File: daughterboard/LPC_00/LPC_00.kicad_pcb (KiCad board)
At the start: 4 copper layers, 67 x 50 mm, 2 parts, among them J1 m2_keyA_67pin_daughterboard

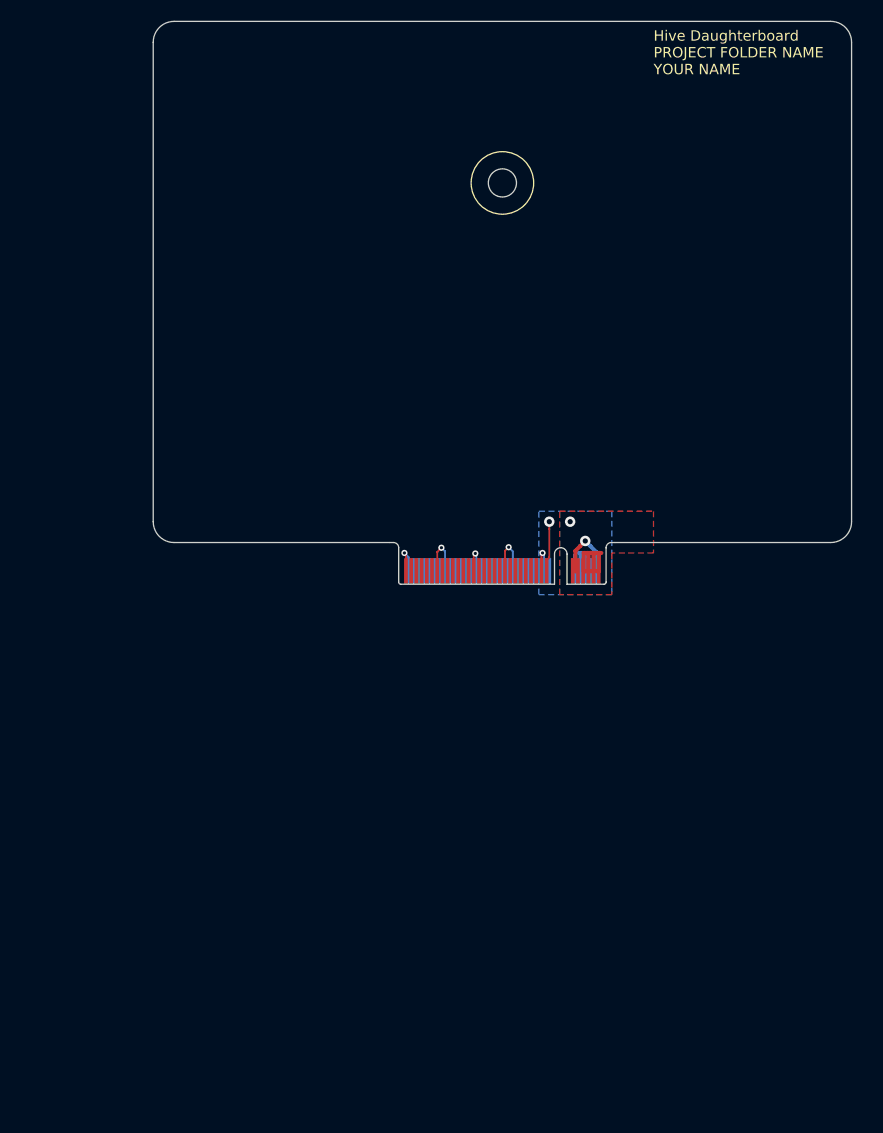
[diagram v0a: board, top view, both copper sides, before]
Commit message: sarted with LPC daughterboard layout
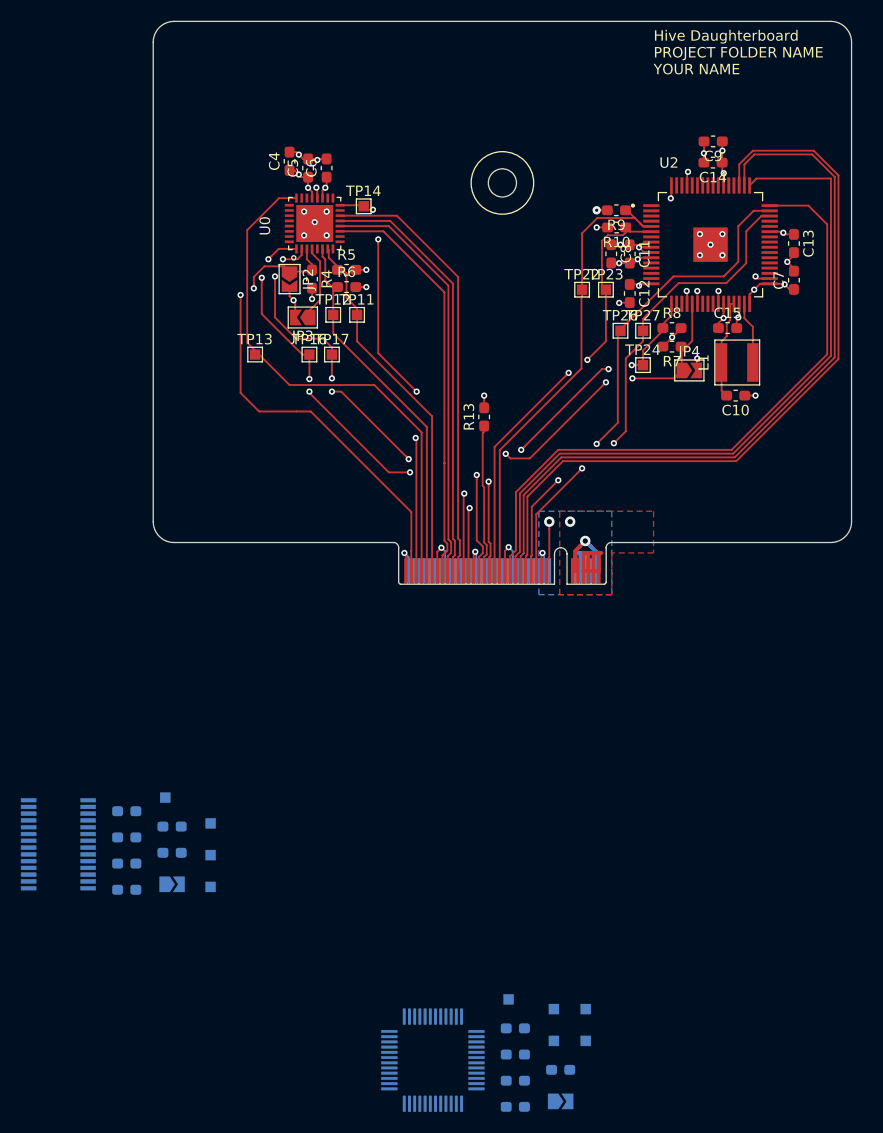
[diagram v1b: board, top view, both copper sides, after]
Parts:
- added C1: 4.7u, Capacitor_SMD:C_0603_1608Metric_Pad1.05x0.95mm_HandSolder, B.Cu at (112.5, 152.8)
- added C10: 22u, Capacitor_SMD:C_0603_1608Metric_Pad1.05x0.95mm_HandSolder, F.Cu at (170.9, 112.9)
- added C11: 100n, Capacitor_SMD:C_0603_1608Metric_Pad1.05x0.95mm_HandSolder, F.Cu at (160.7, 99.3)
- added C12: 100n, Capacitor_SMD:C_0603_1608Metric_Pad1.05x0.95mm_HandSolder, F.Cu at (160.7, 103.1)
- added C13: 100n, Capacitor_SMD:C_0603_1608Metric_Pad1.05x0.95mm_HandSolder, F.Cu at (176.5, 98.3)
- added C14: 100n, Capacitor_SMD:C_0603_1608Metric_Pad1.05x0.95mm_HandSolder, F.Cu at (168.7, 90.6)
- added C15: 100n, Capacitor_SMD:C_0603_1608Metric_Pad1.05x0.95mm_HandSolder, F.Cu at (170.1, 106.4)
- added C16: 4.7u, Capacitor_SMD:C_0603_1608Metric_Pad1.05x0.95mm_HandSolder, B.Cu at (149.7, 173.6)
- added C17: 100n, Capacitor_SMD:C_0603_1608Metric_Pad1.05x0.95mm_HandSolder, B.Cu at (154.1, 177.6)
- added C18: 100n, Capacitor_SMD:C_0603_1608Metric_Pad1.05x0.95mm_HandSolder, B.Cu at (149.7, 176.1)
- added C2: 100n, Capacitor_SMD:C_0603_1608Metric_Pad1.05x0.95mm_HandSolder, B.Cu at (112.5, 160.3)
- added C3: 100n, Capacitor_SMD:C_0603_1608Metric_Pad1.05x0.95mm_HandSolder, B.Cu at (116.8, 154.3)
- added C4: 4.7u, Capacitor_SMD:C_0603_1608Metric_Pad1.05x0.95mm_HandSolder, F.Cu at (128.1, 90.4)
- added C5: 100n, Capacitor_SMD:C_0603_1608Metric_Pad1.05x0.95mm_HandSolder, F.Cu at (129.9, 91.1)
- added C6: 100n, Capacitor_SMD:C_0603_1608Metric_Pad1.05x0.95mm_HandSolder, F.Cu at (131.6, 91.1)
- added C7: 22u, Capacitor_SMD:C_0603_1608Metric_Pad1.05x0.95mm_HandSolder, F.Cu at (176.5, 101.8)
- added C8: 100n, Capacitor_SMD:C_0603_1608Metric_Pad1.05x0.95mm_HandSolder, F.Cu at (158.9, 99.3)
- added C9: 47p, Capacitor_SMD:C_0603_1608Metric_Pad1.05x0.95mm_HandSolder, F.Cu at (168.7, 88.5)
- added JP1: NRST, Jumper:SolderJumper-2_P1.3mm_Open_TrianglePad1.0x1.5mm, B.Cu at (116.8, 159.8)
- added JP2: NRST, Jumper:SolderJumper-2_P1.3mm_Open_TrianglePad1.0x1.5mm, F.Cu at (128.1, 101.7)
- added JP3: NJRST, Jumper:SolderJumper-2_P1.3mm_Open_TrianglePad1.0x1.5mm, F.Cu at (129.4, 105.4)
- added JP4: NRST, Jumper:SolderJumper-2_P1.3mm_Open_TrianglePad1.0x1.5mm, F.Cu at (166.4, 110.5)
- added JP5: NRST, Jumper:SolderJumper-2_P1.3mm_Open_TrianglePad1.0x1.5mm, B.Cu at (154.1, 180.6)
- added L1: 4.7u, hive_daughterboard:TYA40204R7M-10, F.Cu at (171.0, 109.7)
- added R1: 100k, Resistor_SMD:R_0603_1608Metric_Pad1.05x0.95mm_HandSolder, B.Cu at (112.5, 157.8)
- added R10: 10k, Resistor_SMD:R_0603_1608Metric_Pad1.05x0.95mm_HandSolder, F.Cu at (159.5, 96.8)
- added R11: 100k, Resistor_SMD:R_0603_1608Metric_Pad1.05x0.95mm_HandSolder, B.Cu at (149.7, 178.6)
- added R12: 100k, Resistor_SMD:R_0603_1608Metric_Pad1.05x0.95mm_HandSolder, B.Cu at (149.7, 181.1)
- added R13: 100k, Resistor_SMD:R_0603_1608Metric_Pad1.05x0.95mm_HandSolder, F.Cu at (146.8, 114.9)
- added R2: 100k, Resistor_SMD:R_0603_1608Metric_Pad1.05x0.95mm_HandSolder, B.Cu at (112.5, 155.3)
- added R3: 100k, Resistor_SMD:R_0603_1608Metric_Pad1.05x0.95mm_HandSolder, B.Cu at (116.8, 156.8)
- added R4: 100k, Resistor_SMD:R_0603_1608Metric_Pad1.05x0.95mm_HandSolder, F.Cu at (130.2, 101.7)
- added R5: 10k, Resistor_SMD:R_0603_1608Metric_Pad1.05x0.95mm_HandSolder, F.Cu at (133.6, 100.8)
- added R6: 10k, Resistor_SMD:R_0603_1608Metric_Pad1.05x0.95mm_HandSolder, F.Cu at (133.6, 102.5)
- added R7: 100k, Resistor_SMD:R_0603_1608Metric_Pad1.05x0.95mm_HandSolder, F.Cu at (164.8, 108.2)
- added R8: 10k, Resistor_SMD:R_0603_1608Metric_Pad1.05x0.95mm_HandSolder, F.Cu at (164.8, 106.4)
- added R9: 10k, Resistor_SMD:R_0603_1608Metric_Pad1.05x0.95mm_HandSolder, F.Cu at (159.4, 95.1)
- added TP1: SWDIO, TestPoint:TestPoint_Pad_1.0x1.0mm, B.Cu at (120.5, 160.0)
- added TP11: SWDIO-TMS, TestPoint:TestPoint_Pad_1.0x1.0mm, F.Cu at (134.6, 105.2)
- added TP12: SWCLK-TCLK, TestPoint:TestPoint_Pad_1.0x1.0mm, F.Cu at (132.3, 105.2)
- added TP13: TDO, TestPoint:TestPoint_Pad_1.0x1.0mm, F.Cu at (124.8, 109.0)
- added TP14: TDI, TestPoint:TestPoint_Pad_1.0x1.0mm, F.Cu at (135.2, 94.7)
- added TP16: USART_TX, TestPoint:TestPoint_Pad_1.0x1.0mm, F.Cu at (130.0, 109.0)
- added TP17: USART_RX, TestPoint:TestPoint_Pad_1.0x1.0mm, F.Cu at (132.1, 109.0)
- added TP2: SWCLK, TestPoint:TestPoint_Pad_1.0x1.0mm, B.Cu at (120.5, 157.0)
- added TP22: SWDIO, TestPoint:TestPoint_Pad_1.0x1.0mm, F.Cu at (156.1, 102.7)
- added TP23: SWCLK, TestPoint:TestPoint_Pad_1.0x1.0mm, F.Cu at (158.4, 102.7)
- added TP24: SWO, TestPoint:TestPoint_Pad_1.0x1.0mm, F.Cu at (162.0, 110.0)
- added TP26: USART_TX, TestPoint:TestPoint_Pad_1.0x1.0mm, F.Cu at (159.8, 106.7)
- added TP27: USART_RX, TestPoint:TestPoint_Pad_1.0x1.0mm, F.Cu at (162.0, 106.7)
- added TP32: SWDIO, TestPoint:TestPoint_Pad_1.0x1.0mm, B.Cu at (153.4, 174.8)
- added TP33: SWCLK, TestPoint:TestPoint_Pad_1.0x1.0mm, B.Cu at (149.1, 170.8)
- added TP34: SWO, TestPoint:TestPoint_Pad_1.0x1.0mm, B.Cu at (153.4, 171.8)
- added TP36: USART_TX, TestPoint:TestPoint_Pad_1.0x1.0mm, B.Cu at (156.5, 174.8)
- added TP37: USART_RX, TestPoint:TestPoint_Pad_1.0x1.0mm, B.Cu at (156.5, 171.8)
- added TP5: USART_TX, TestPoint:TestPoint_Pad_1.0x1.0mm, B.Cu at (116.2, 151.5)
- added TP6: USART_RX, TestPoint:TestPoint_Pad_1.0x1.0mm, B.Cu at (120.5, 153.9)
- added U0: LPC845M301JHI33Y, hive_daughterboard:LPC845M301JHI33Y, F.Cu at (130.5, 96.4)
- added U1: LPC1114FDH28_102_5, hive_daughterboard:LPC1114FDH28_1025, B.Cu at (105.9, 155.9)
- added U2: LPC55S69JBD64K, hive_daughterboard:LPC55S69JBD64K, F.Cu at (168.5, 98.4)
- added U3: LPC1313FBD48_01,15, hive_daughterboard:LPC1313FBD48_0115, B.Cu at (141.8, 176.7)
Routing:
- net /Target 2/GPIO2.3: track 0.00 -> 73.2 mm
- net /Target 2/GPIO2.2: track 0.00 -> 72.0 mm
- net /Target 2/GPIO2.1: track 0.00 -> 68.0 mm
- net /Target 2/GPIO2.0: track 0.00 -> 61.9 mm
- net /Target 0/TDO|SWO_0: track 0.00 -> 50.7 mm
- net /Target 2/UART_TxD2: track 0.00 -> 48.0 mm, vias 0 -> 2
- net /Target 2/UART_RxD2: track 0.00 -> 47.6 mm, vias 0 -> 2
- net /Target 0/RST_0: track 0.00 -> 47.3 mm, vias 0 -> 2
- net /Target 2/TMS|SWDIO_2: track 0.00 -> 44.5 mm
- net /Target 0/UART_RxD0: track 0.00 -> 44.5 mm, vias 0 -> 6
- net /Target 0/UART_TxD0: track 0.00 -> 43.6 mm, vias 0 -> 6
- net /Target 2/TCK|SWDCLK_2: track 0.00 -> 42.3 mm, vias 0 -> 2
- net /Target 0/GPIO0.3: track 0.00 -> 42.1 mm
- net /Target 0/GPIO0.2: track 0.00 -> 41.1 mm
- net /Target 2/RST_2: track 0.00 -> 41.0 mm, vias 0 -> 4
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
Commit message: further work on LPC layout
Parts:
- moved C2 51.0 mm to (130.0, 112.4)
- moved R2 48.2 mm to (143.6, 118.5), turned to 90 degrees
- moved C1 45.8 mm to (130.0, 110.5)
- moved R3 45.8 mm to (141.9, 118.5), turned to 90 degrees
- moved U1 45.1 mm to (129.1, 117.2), turned to 270 degrees
- moved TP1 44.0 mm to (135.8, 118.7)
- moved TP2 42.1 mm to (138.1, 118.7)
- moved JP1 40.5 mm to (120.3, 119.5), turned to 270 degrees
- moved R1 39.8 mm to (122.9, 119.4), turned to 270 degrees
- moved TP6 34.6 mm to (135.1, 122.6)
- moved C3 34.6 mm to (130.0, 122.3)
- moved TP5 33.4 mm to (132.8, 122.6)
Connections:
- C1 pad 1: Net-(C1-Pad1) -> +3V3
- C2 pad 1: Net-(C1-Pad1) -> +3V3
- C3 pad 1: Net-(C1-Pad1) -> +3V3
- U1 pad 21: Net-(C1-Pad1) -> +3V3
- U1 pad 7: Net-(C1-Pad1) -> +3V3
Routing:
- net /Target 1/RST_1: track 0.00 -> 42.5 mm, vias 0 -> 2
- net /Target 1/TCK|SWDCLK_1: track 0.00 -> 27.6 mm, vias 0 -> 2
- net /Target 1/GPIO1.3: track 0.00 -> 23.3 mm
- net /Target 1/GPIO1.1: track 0.00 -> 23.2 mm
- net /Target 1/GPIO1.2: track 0.00 -> 23.2 mm
- net /Target 1/GPIO1.0: track 0.00 -> 23.0 mm
- net /Target 1/TMS|SWDIO_1: track 0.00 -> 21.5 mm
- net /Target 1/UART_RxD1: track 0.00 -> 14.4 mm, vias 0 -> 2
- net /Target 1/UART_TxD1: track 0.00 -> 13.4 mm, vias 0 -> 2
- net GND: track 60.4 -> 72.3 mm, vias 36 -> 40
- net /Target 1/TDO|SWO_1: track 0.00 -> 11.6 mm
- net /Target 1/TDI|NC_1: track 0.00 -> 11.2 mm
- net +3V3: track 48.8 -> 55.8 mm, vias 19 -> 23

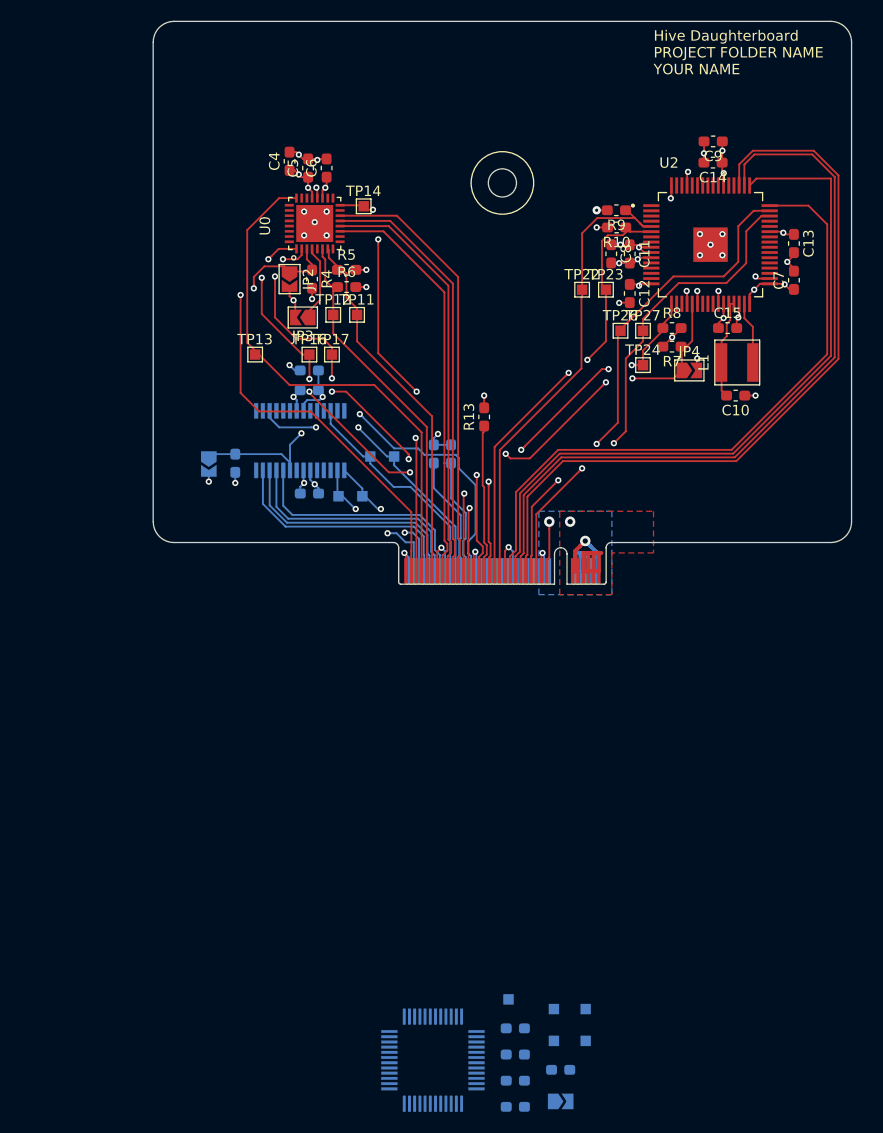
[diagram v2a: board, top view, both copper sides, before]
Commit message: finsihed LPC daughterboard layout
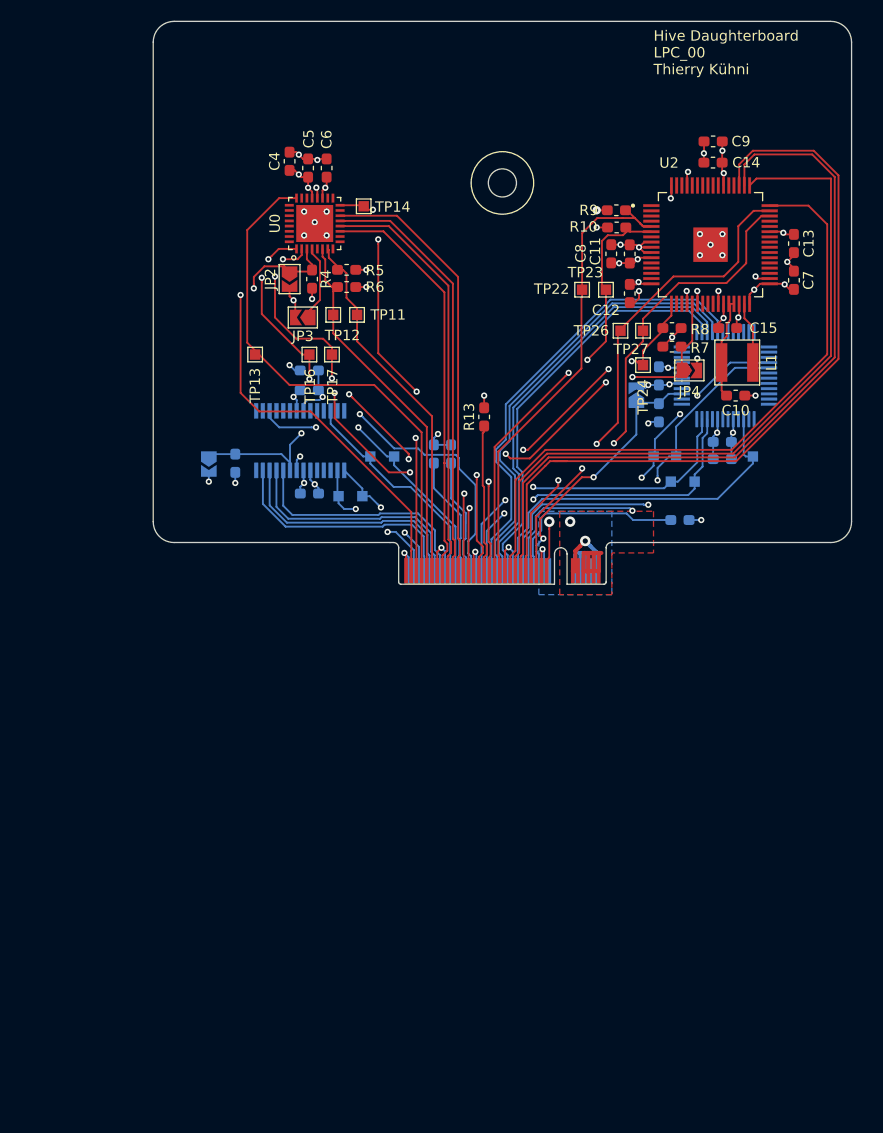
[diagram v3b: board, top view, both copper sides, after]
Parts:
- moved U3 71.4 mm to (169.9, 111.0)
- moved JP5 68.1 mm to (161.4, 112.9), turned to 90 degrees
- moved C17 67.2 mm to (163.5, 111.0), turned to 270 degrees
- moved R11 65.5 mm to (163.5, 114.6), turned to 270 degrees
- moved C18 62.0 mm to (169.6, 117.3)
- moved TP32 59.2 mm to (172.5, 118.7)
- moved R12 58.5 mm to (165.5, 124.8)
- moved C16 58.1 mm to (169.6, 119.0)
- moved TP33 54.5 mm to (165.2, 118.7)
- moved TP36 54.3 mm to (164.7, 121.2)
- moved TP34 53.9 mm to (163.0, 118.7)
- moved TP37 51.7 mm to (166.9, 121.2)
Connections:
- U3 pad 11: /Target 3/GPIO3.0 -> Net-(U3-Pad11)
- U3 pad 12: /Target 3/GPIO3.1 -> Net-(U3-Pad12)
- U3 pad 14: Net-(U3-Pad14) -> /Target 3/GPIO3.0
- U3 pad 15: Net-(U3-Pad15) -> /Target 3/GPIO3.1
- U3 pad 16: Net-(U3-Pad16) -> /Target 3/GPIO3.2
- U3 pad 17: Net-(U3-Pad17) -> /Target 3/GPIO3.3
- U3 pad 24: /Target 3/GPIO3.2 -> Net-(U3-Pad24)
- U3 pad 25: /Target 3/GPIO3.3 -> Net-(U3-Pad25)
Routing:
- net /Target 3/GPIO3.3: track 0.00 -> 44.2 mm
- net /Target 3/GPIO3.2: track 0.00 -> 43.0 mm
- net /Target 3/GPIO3.1: track 0.00 -> 41.0 mm
- net /Target 3/GPIO3.0: track 0.00 -> 39.7 mm
- net /Target 3/TCK|SWDCLK_3: track 0.00 -> 37.6 mm, vias 0 -> 2
- net /Target 3/TDO|SWO_3: track 0.00 -> 37.2 mm, vias 0 -> 4
- net /Target 3/TMS|SWDIO_3: track 0.00 -> 34.5 mm
- net /Target 3/UART_TxD3: track 0.00 -> 32.7 mm, vias 0 -> 2
- net /Target 3/UART_RxD3: track 0.00 -> 32.1 mm, vias 0 -> 2
- net /Target 3/RST_3: track 0.00 -> 25.9 mm, vias 0 -> 2
- net /Target 3/TDI|NC_3: track 0.00 -> 18.4 mm
- net GND: track 72.3 -> 85.3 mm, vias 40 -> 45
- net +3V3: track 55.8 -> 63.1 mm, vias 23 -> 26
- net /Target 2/GPIO2.3: track 73.2 -> 75.5 mm
- net /Target 0/UART_TxD0: track 43.9 -> 43.1 mm
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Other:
- board text added: "Hive Daughterboard LPC_00 Thierry Kühni"
- board text removed: "Hive Daughterboard PROJECT FOLDER NAME YOUR NAME"

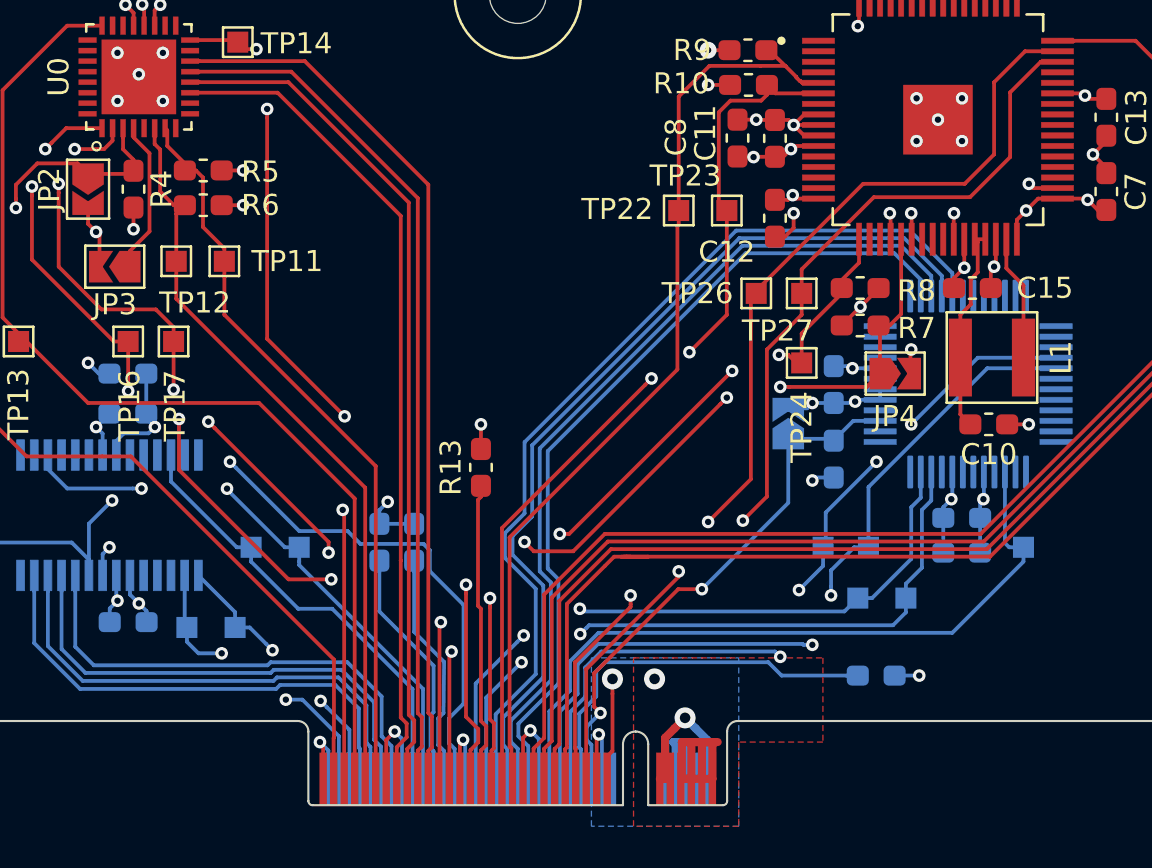
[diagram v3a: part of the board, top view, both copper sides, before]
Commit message: length matching daughterboards
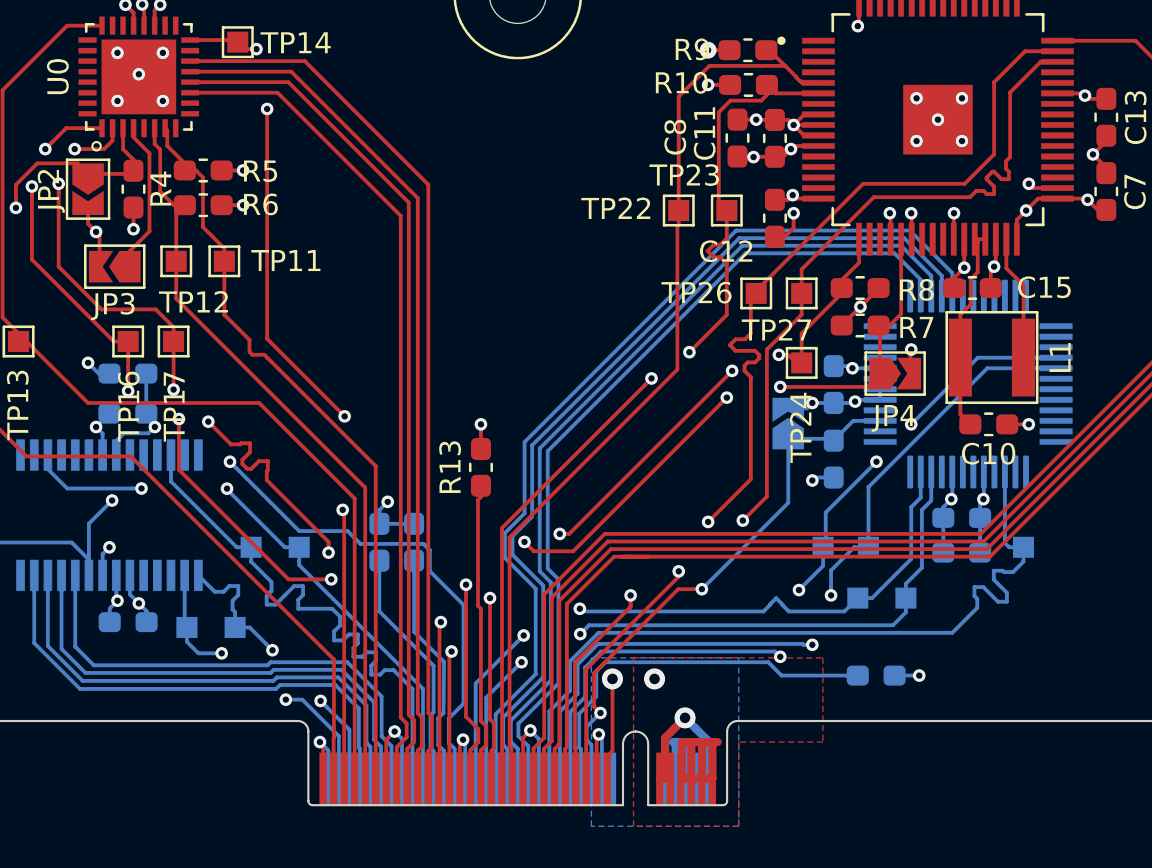
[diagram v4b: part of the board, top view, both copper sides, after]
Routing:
- net /Target 1/TMS|SWDIO_1: track 21.5 -> 27.6 mm
- net /Target 3/TMS|SWDIO_3: track 34.5 -> 37.7 mm
- net /Target 2/UART_RxD2: track 47.6 -> 50.0 mm
- net /Target 2/UART_TxD2: track 48.1 -> 50.1 mm
- net /Target 0/UART_TxD0: track 43.1 -> 45.2 mm
- net /Target 1/UART_TxD1: track 13.0 -> 14.3 mm
- net /Target 2/TCK|SWDCLK_2: track 42.3 -> 43.4 mm
- net /Target 3/UART_RxD3: track 32.1 -> 32.7 mm
